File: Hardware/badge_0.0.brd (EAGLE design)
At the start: 100 x 50 mm, 43 parts, among them CON1 PH_2, IC1 CP2102, J3 2X6 FEMALE, SW1 MK12C02, SW2 MK12C02, U4 MCP73832T-2DCI/OT

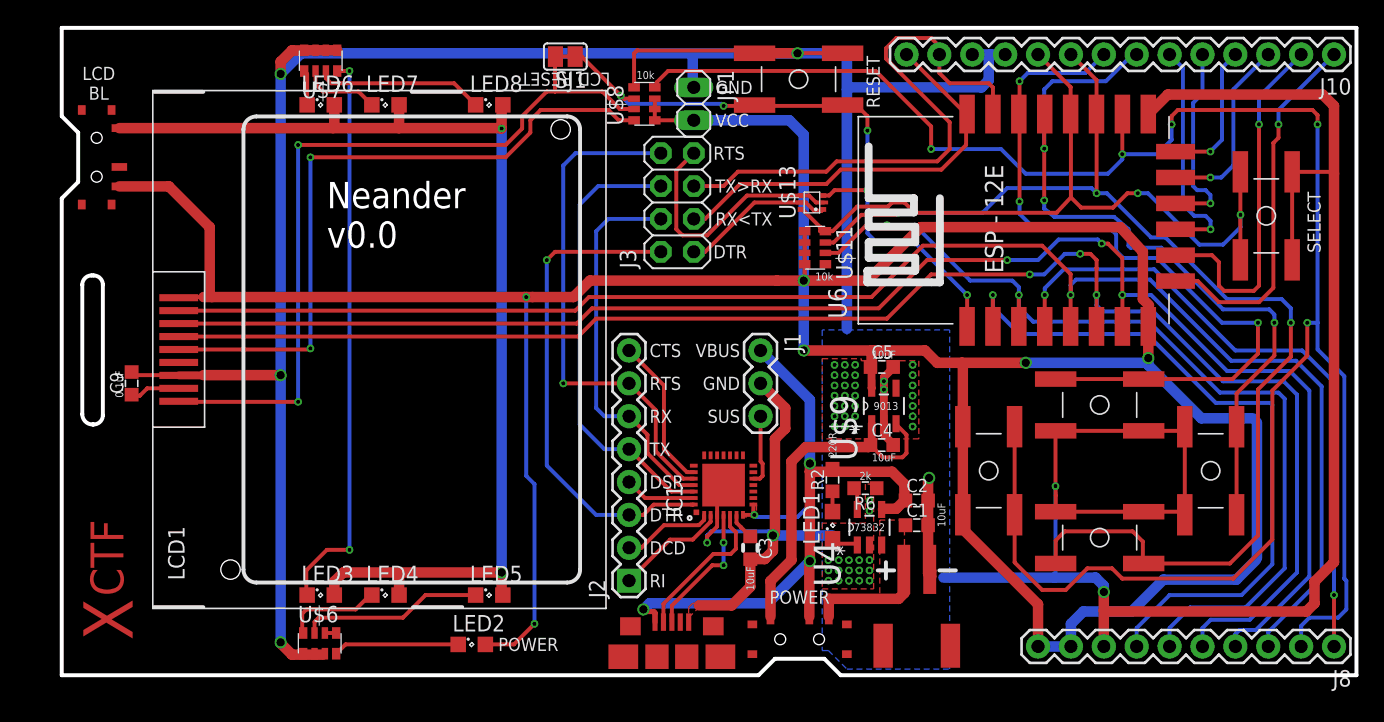
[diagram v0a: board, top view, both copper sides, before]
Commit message: Swapped a silks, added more silks, bit of routing changes
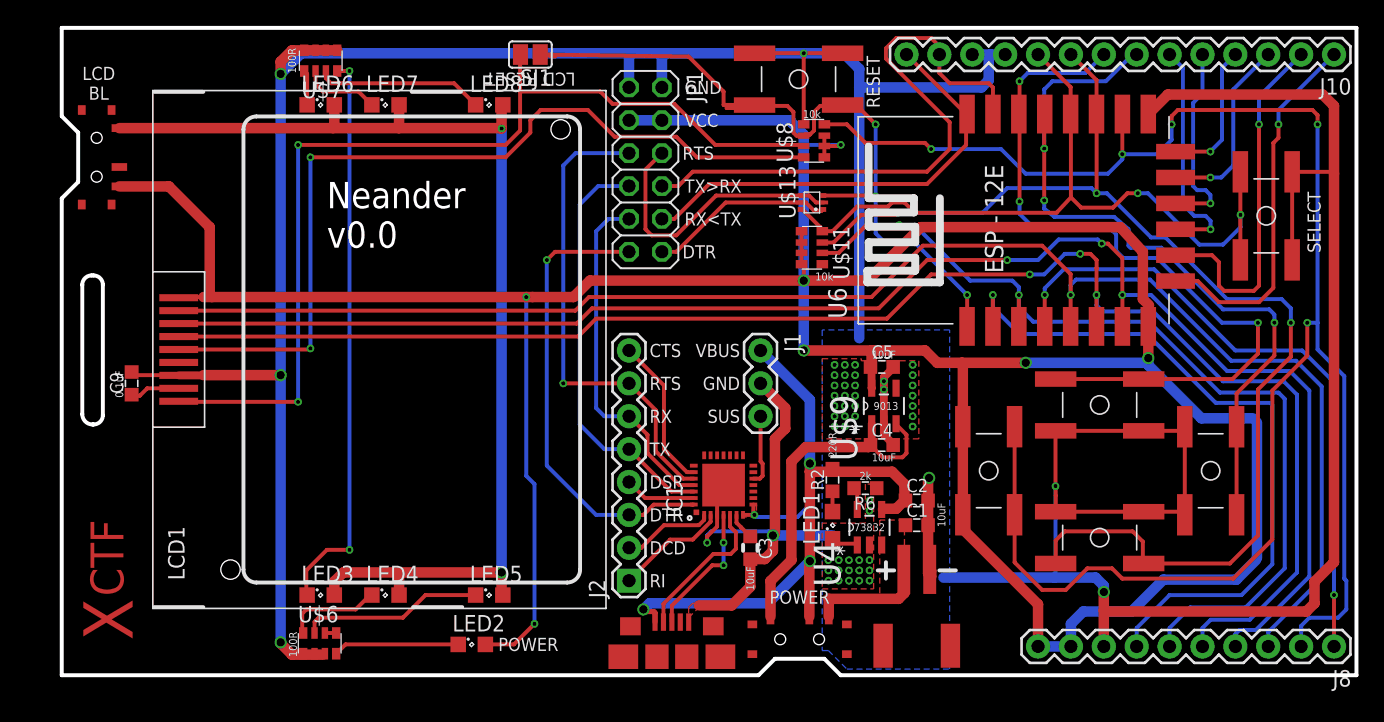
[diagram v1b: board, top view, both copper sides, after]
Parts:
- removed J3: 2X6 FEMALE, adafruit:2X04
- JP1: device pinhead:1X02 -> pinhead:2X06
- moved U$8 13.4 mm to (58.1, 41.3)
- moved JP1 6.30 mm to (45.1, 39.1)
- moved SJ1 2.70 mm to (36.2, 47.9)
- moved U$11 0.24 mm to (57.9, 33.0)
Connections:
- net AUTO_DTR: now also JP1.12; no longer J3.1
- net AUTO_RTS: now also JP1.6; no longer J3.7
- net GND: now also JP1.2
- net RX: now also JP1.8; no longer J3.5
- net S_DTR: now also JP1.11; no longer J3.2
- net S_RTS: now also JP1.5; no longer J3.8
- net S_RXD: now also JP1.9; no longer J3.4
- net S_TXD: now also JP1.7; no longer J3.6
- net TX: now also JP1.10; no longer J3.3
- net VCC: now also JP1.3, JP1.4; no longer JP1.2
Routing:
- net GPIO15/SPI_CS: track 159.7 -> 143.2 mm
- net LCD_RESET: track 60.6 -> 76.5 mm
- net N$3: track 52.4 -> 66.7 mm
- net RESET: track 52.1 -> 61.9 mm, vias 5 -> 3
- net GND: track 363.3 -> 358.1 mm
- net VCC: track 263.0 -> 267.4 mm, vias 6 -> 7
- net TX: track 32.4 -> 34.9 mm
- net S_RTS: track 39.8 -> 37.3 mm
- net S_DTR: track 38.2 -> 35.7 mm
- net AUTO_DTR: track 11.9 -> 14.3 mm
- net S_TXD: track 34.8 -> 32.3 mm
- net S_RXD: track 29.9 -> 27.4 mm
- net RX: track 44.2 -> 46.7 mm
- net AUTO_RTS: track 19.5 -> 21.9 mm
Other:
- board text added: "100R"

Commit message: Moved a bit of stuff to prevent stop-mask errors, and one dimension error
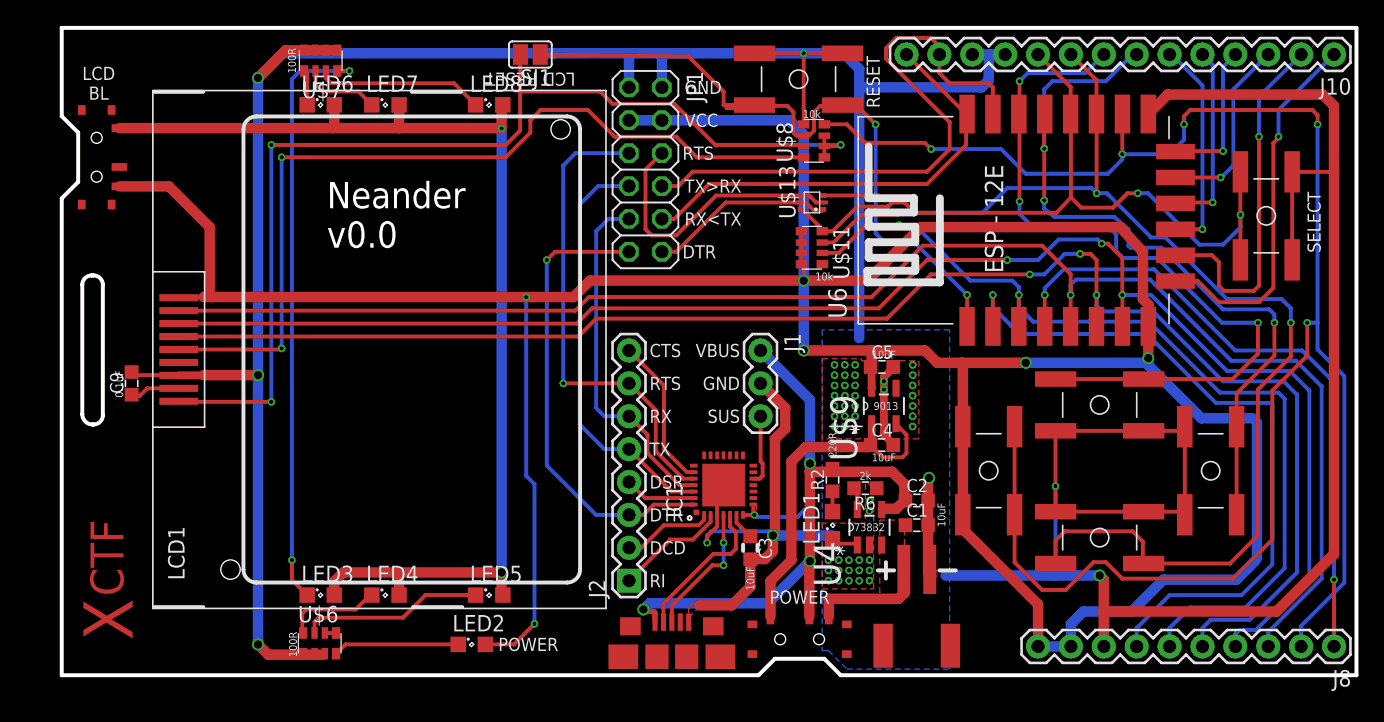
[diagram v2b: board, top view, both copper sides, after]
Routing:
- net N$14: track 43.9 -> 46.0 mm
- net GND: track 358.1 -> 360.0 mm
- net GPIO9: track 18.0 -> 16.7 mm
- net GPIO15/SPI_CS: track 143.2 -> 142.1 mm
- net GPIO10: track 15.4 -> 14.7 mm
- net SCLK: track 11.0 -> 11.5 mm

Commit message: added some changes from YS
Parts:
- added SJ2: SOLDERJUMPERTRACE, SparkFun-Retired:SJ_2S-TRACE
- SJ1: value (none) -> SOLDERJUMPERTRACE; device jumper:SJ -> SparkFun-Retired:SJ_2S-TRACE
- moved SJ1 0.32 mm to (35.9, 47.9)
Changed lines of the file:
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@@
 <?xml version="1.0" encoding="utf-8"?>
 <!DOCTYPE eagle SYSTEM "eagle.dtd">
-<eagle version="7.1.0">
+<eagle version="7.5.0">
 <drawing>
 <settings>
@@
 <element name="U$12" library="badge" package="EVQQWN03W" value="TOUCHSWITCH" x="56.911875" y="46.0375" smashed="yes" rot="R270"/>
 <element name="U$13" library="LYS_special" package="SOT666" value="PEMH9,115" x="57.94375" y="36.5125" rot="R90"/>
-<element name="SJ1" library="jumper" package="SJ" value="" x="36.195" y="47.9425" rot="R180"/>
+<element name="SJ1" library="SparkFun-Retired" package="SJ_2S-TRACE" value="SOLDERJUMPERTRACE" x="35.8775" y="47.9425" rot="R180"/>
 <element name="JP1" library="pinhead" package="2X06" value="" x="45.085" y="39.0525" rot="R270"/>
+<element name="SJ2" library="SparkFun-Retired" package="SJ_2S-TRACE" value="SOLDERJUMPERTRACE" x="-1.5875" y="0.9525"/>
 </elements>
 <signals>
@@
 <contactref element="U$8" pad="6"/>
 <contactref element="SJ1" pad="1"/>
-<wire x1="38.1" y1="47.78375" x2="36.957" y2="47.9425" width="0.3048" layer="1"/>
 <wire x1="62.865" y1="37.0505" x2="62.865" y2="36.98875" width="0.3048" layer="1"/>
 <via x="62.865" y="36.98875" extent="1-16" drill="0.3048" shape="octagon"/>
@@
 <wire x1="54.61" y1="43.815" x2="51.353125" y2="43.815" width="0.3048" layer="1"/>
 <wire x1="51.353125" y1="43.815" x2="53.511875" y2="44.0375" width="0.3048" layer="1"/>
-<wire x1="36.957" y1="47.9425" x2="48.41875" y2="47.78375" width="0.3048" layer="1"/>
 <wire x1="48.41875" y1="47.78375" x2="51.1175" y2="45.085" width="0.3048" layer="1"/>
 <wire x1="51.1175" y1="45.085" x2="51.1175" y2="44.050625" width="0.3048" layer="1"/>
 <wire x1="51.1175" y1="44.050625" x2="53.511875" y2="44.0375" width="0.3048" layer="1"/>
+<wire x1="48.41875" y1="47.78375" x2="36.3855" y2="47.78375" width="0.3048" layer="1"/>
+<wire x1="36.3855" y1="47.78375" x2="36.3855" y2="47.9425" width="0.3048" layer="1"/>
 </signal>
 <signal name="ADC">
@@
 <wire x1="41.5925" y1="45.085" x2="35.40125" y2="45.085" width="0.3048" layer="1"/>
 <wire x1="35.40125" y1="45.085" x2="35.40125" y2="48.0695" width="0.3048" layer="1"/>
-<wire x1="35.40125" y1="48.0695" x2="35.433" y2="47.9425" width="0.3048" layer="1"/>
+<wire x1="35.40125" y1="48.0695" x2="35.3695" y2="47.9425" width="0.3048" layer="1"/>
 <wire x1="35.40125" y1="45.085" x2="35.40125" y2="42.06875" width="0.3048" layer="1"/>
 <wire x1="35.40125" y1="42.06875" x2="34.29" y2="40.9575" width="0.3048" layer="1"/>

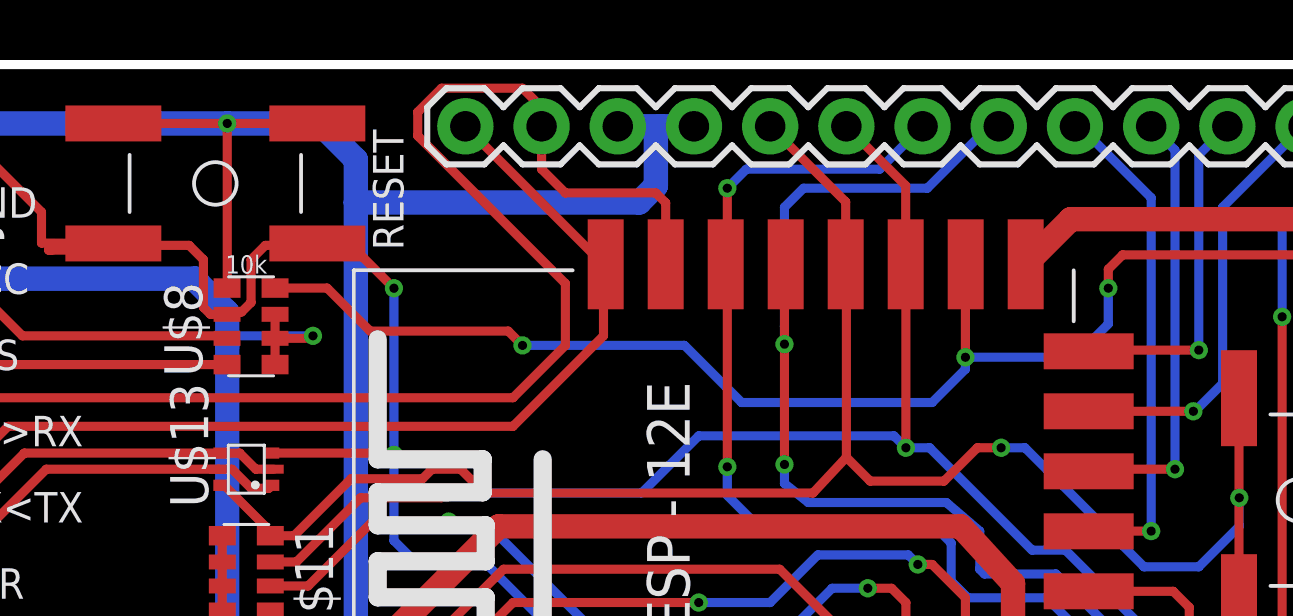
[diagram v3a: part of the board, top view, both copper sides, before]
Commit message: Paralleled GND trace, rerouted reset trace for wider separation
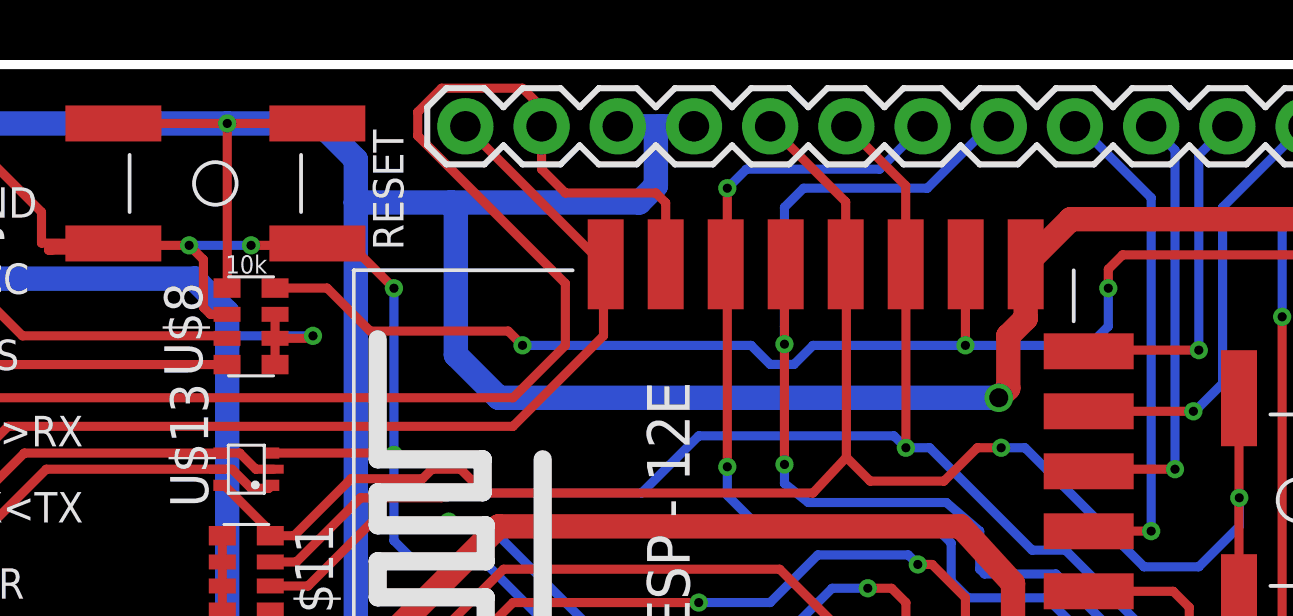
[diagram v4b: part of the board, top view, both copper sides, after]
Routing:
- net GND: track 360.0 -> 388.7 mm, vias 55 -> 56
- net GPIO15/SPI_CS: track 142.1 -> 140.5 mm
- net RESET: track 61.5 -> 61.1 mm, vias 3 -> 5
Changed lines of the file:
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@@
 <?xml version="1.0" encoding="utf-8"?>
 <!DOCTYPE eagle SYSTEM "eagle.dtd">
-<eagle version="7.5.0">
+<eagle version="7.1.0">
 <drawing>
 <settings>
@@
 <wire x1="57.30875" y1="42.55" x2="57.30875" y2="47.87875" width="0.3048" layer="1"/>
 <wire x1="57.30875" y1="47.87875" x2="57.4675" y2="48.0375" width="0.3048" layer="1"/>
-<wire x1="71.040625" y1="45.4025" x2="61.595" y2="45.4025" width="0.8128" layer="16"/>
+<wire x1="71.040625" y1="45.4025" x2="64.77" y2="45.4025" width="0.8128" layer="16"/>
+<wire x1="64.77" y1="45.4025" x2="61.595" y2="45.4025" width="0.8128" layer="16"/>
 <wire x1="61.595" y1="45.4025" x2="61.595" y2="26.035" width="0.8128" layer="16"/>
 <wire x1="60.38875" y1="48.0375" x2="61.595" y2="46.83125" width="0.8128" layer="16"/>
@@
 <wire x1="17.07" y1="48.0375" x2="15.160625" y2="46.128125" width="0.8128" layer="16"/>
 <wire x1="17.2925" y1="48.26" x2="15.160625" y2="46.128125" width="0.8128" layer="1"/>
+<wire x1="83.92375" y1="43.3425" x2="83.92375" y2="41.5375" width="0.8128" layer="1"/>
+<wire x1="83.92375" y1="41.5375" x2="83.34375" y2="40.9575" width="0.8128" layer="1"/>
+<wire x1="83.34375" y1="40.9575" x2="83.34375" y2="39.21125" width="0.8128" layer="1"/>
+<wire x1="83.34375" y1="39.21125" x2="83.02625" y2="38.89375" width="0.8128" layer="1"/>
+<via x="83.02625" y="38.89375" extent="1-16" drill="0.635" shape="octagon"/>
+<wire x1="83.02625" y1="38.89375" x2="66.3575" y2="38.89375" width="0.8128" layer="16"/>
+<wire x1="66.3575" y1="38.89375" x2="64.92875" y2="40.3225" width="0.8128" layer="16"/>
+<wire x1="64.92875" y1="40.3225" x2="64.92875" y2="45.24375" width="0.8128" layer="16"/>
+<wire x1="64.92875" y1="45.24375" x2="64.77" y2="45.4025" width="0.8128" layer="16"/>
 </signal>
 <signal name="N$3">
@@
 <wire x1="95.72625" y1="3.81" x2="95.72625" y2="2.2225" width="0.3048" layer="16"/>
 <contactref element="U$8" pad="4"/>
-<via x="81.915" y="40.243125" extent="1-16" drill="0.3048" shape="octagon"/>
-<wire x1="81.915" y1="40.243125" x2="81.915" y2="43.33375" width="0.3048" layer="1"/>
+<via x="81.915" y="40.64" extent="1-16" drill="0.3048" shape="octagon"/>
+<wire x1="81.915" y1="40.64" x2="81.915" y2="43.33375" width="0.3048" layer="1"/>
 <wire x1="81.915" y1="43.33375" x2="81.92375" y2="43.3425" width="0.3048" layer="1"/>
-<wire x1="81.915" y1="40.243125" x2="85.56625" y2="40.243125" width="0.3048" layer="16"/>
-<wire x1="85.56625" y1="40.243125" x2="86.6775" y2="41.354375" width="0.3048" layer="16"/>
-<wire x1="86.6775" y1="41.354375" x2="86.6775" y2="42.545" width="0.3048" layer="16"/>
+<wire x1="81.915" y1="40.64" x2="86.0425" y2="40.64" width="0.3048" layer="16"/>
+<wire x1="86.0425" y1="40.64" x2="86.6775" y2="41.275" width="0.3048" layer="16"/>
+<wire x1="86.6775" y1="41.275" x2="86.6775" y2="42.545" width="0.3048" layer="16"/>
 <via x="86.6775" y="42.545" extent="1-16" drill="0.3048" shape="octagon"/>
 <wire x1="86.6775" y1="42.545" x2="86.6775" y2="43.18" width="0.3048" layer="1"/>
@@
 <wire x1="73.59625" y1="12.395625" x2="73.59625" y2="8.715625" width="0.3048" layer="1"/>
 <wire x1="73.59625" y1="8.715625" x2="75.72375" y2="6.588125" width="0.3048" layer="1"/>
-<wire x1="81.915" y1="39.84625" x2="80.80375" y2="38.735" width="0.3048" layer="16"/>
-<wire x1="80.80375" y1="38.735" x2="74.45375" y2="38.735" width="0.3048" layer="16"/>
-<wire x1="74.45375" y1="38.735" x2="72.54875" y2="40.64" width="0.3048" layer="16"/>
-<wire x1="72.54875" y1="40.64" x2="67.15125" y2="40.64" width="0.3048" layer="16"/>
+<wire x1="74.77125" y1="40.64" x2="67.15125" y2="40.64" width="0.3048" layer="16"/>
 <via x="67.15125" y="40.64" extent="1-16" drill="0.3048" shape="octagon"/>
-<wire x1="81.915" y1="39.84625" x2="81.915" y2="40.243125" width="0.3048" layer="16"/>
 <wire x1="75.72375" y1="6.588125" x2="77.549375" y2="6.588125" width="0.3048" layer="1"/>
 <wire x1="77.549375" y1="6.588125" x2="79.6925" y2="8.73125" width="0.3048" layer="1"/>
@@
 <wire x1="99.06" y1="23.098125" x2="99.06" y2="7.14375" width="0.3048" layer="16"/>
 <wire x1="99.06" y1="7.14375" x2="95.72625" y2="3.81" width="0.3048" layer="16"/>
+<wire x1="74.77125" y1="40.64" x2="75.40625" y2="40.005" width="0.3048" layer="16"/>
+<wire x1="75.40625" y1="40.005" x2="76.2" y2="40.005" width="0.3048" layer="16"/>
+<wire x1="76.2" y1="40.005" x2="76.835" y2="40.64" width="0.3048" layer="16"/>
+<wire x1="76.835" y1="40.64" x2="81.915" y2="40.64" width="0.3048" layer="16"/>
 </signal>
 <signal name="VBUS">
@@
 <wire x1="62.865" y1="37.0505" x2="62.865" y2="36.98875" width="0.3048" layer="1"/>
 <via x="62.865" y="36.98875" extent="1-16" drill="0.3048" shape="octagon"/>
-<wire x1="58.1025" y1="43.4975" x2="58.57875" y2="43.97375" width="0.3048" layer="1"/>
-<wire x1="58.57875" y1="43.97375" x2="60.248125" y2="43.97375" width="0.3048" layer="1"/>
+<wire x1="58.1025" y1="43.97375" x2="60.248125" y2="43.97375" width="0.3048" layer="1"/>
 <wire x1="60.248125" y1="43.97375" x2="60.311875" y2="44.0375" width="0.3048" layer="1"/>
-<wire x1="58.1025" y1="43.4975" x2="58.1025" y2="42.06875" width="0.3048" layer="1"/>
-<wire x1="58.1025" y1="42.06875" x2="57.785" y2="41.75125" width="0.3048" layer="1"/>
-<wire x1="57.785" y1="41.75125" x2="57.37875" y2="41.75125" width="0.3048" layer="1"/>
 <wire x1="57.37875" y1="41.75125" x2="57.3025" y2="41.675" width="0.3048" layer="1"/>
 <wire x1="57.3025" y1="41.675" x2="56.75" y2="41.675" width="0.3048" layer="1"/>
@@
 <wire x1="48.41875" y1="47.78375" x2="36.3855" y2="47.78375" width="0.3048" layer="1"/>
 <wire x1="36.3855" y1="47.78375" x2="36.3855" y2="47.9425" width="0.3048" layer="1"/>
+<via x="58.1025" y="43.97375" extent="1-16" drill="0.3048" shape="octagon"/>
+<wire x1="58.1025" y1="43.97375" x2="56.03875" y2="43.97375" width="0.3048" layer="16"/>
+<via x="56.03875" y="43.97375" extent="1-16" drill="0.3048" shape="octagon"/>
 </signal>
 <signal name="ADC">

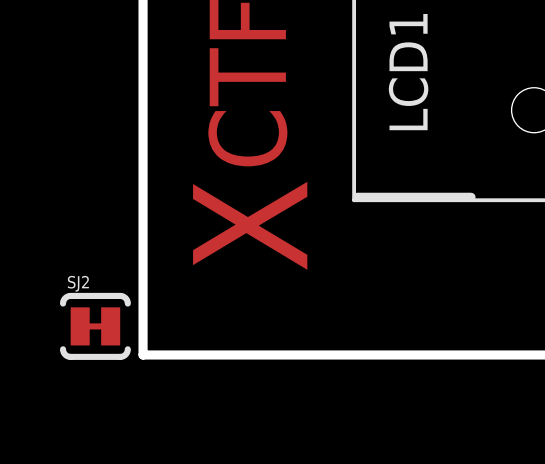
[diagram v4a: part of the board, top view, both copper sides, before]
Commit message: deleted lone component
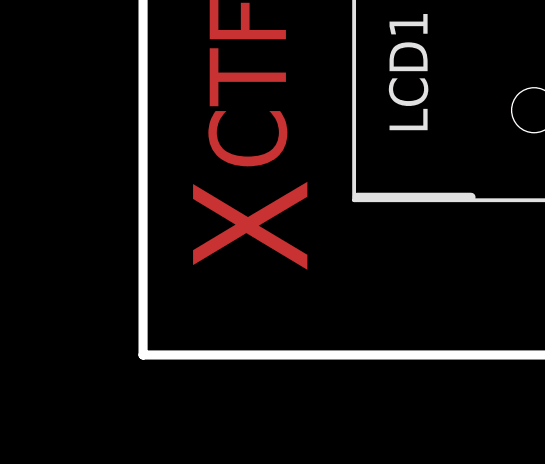
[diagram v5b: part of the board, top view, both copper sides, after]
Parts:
- removed SJ2: SOLDERJUMPERTRACE, SparkFun-Retired:SJ_2S-TRACE
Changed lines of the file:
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@@
 <?xml version="1.0" encoding="utf-8"?>
 <!DOCTYPE eagle SYSTEM "eagle.dtd">
-<eagle version="7.1.0">
+<eagle version="7.5.0">
 <drawing>
 <settings>
@@
 <element name="SJ1" library="SparkFun-Retired" package="SJ_2S-TRACE" value="SOLDERJUMPERTRACE" x="35.8775" y="47.9425" rot="R180"/>
 <element name="JP1" library="pinhead" package="2X06" value="" x="45.085" y="39.0525" rot="R270"/>
-<element name="SJ2" library="SparkFun-Retired" package="SJ_2S-TRACE" value="SOLDERJUMPERTRACE" x="-1.5875" y="0.9525"/>
 </elements>
 <signals>
